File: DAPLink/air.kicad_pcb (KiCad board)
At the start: 2 copper layers, 40.5 x 19.3 mm, 55 parts, among them J1 Conn_01x05, J2 Conn_01x05, J3 Conn_01x04, U1 MT9700, U2 AIR32F103CBT6-LQFP48, U3 RT9013-33GB, U4 USBLC6-2SC6, Y1 8M/20pF

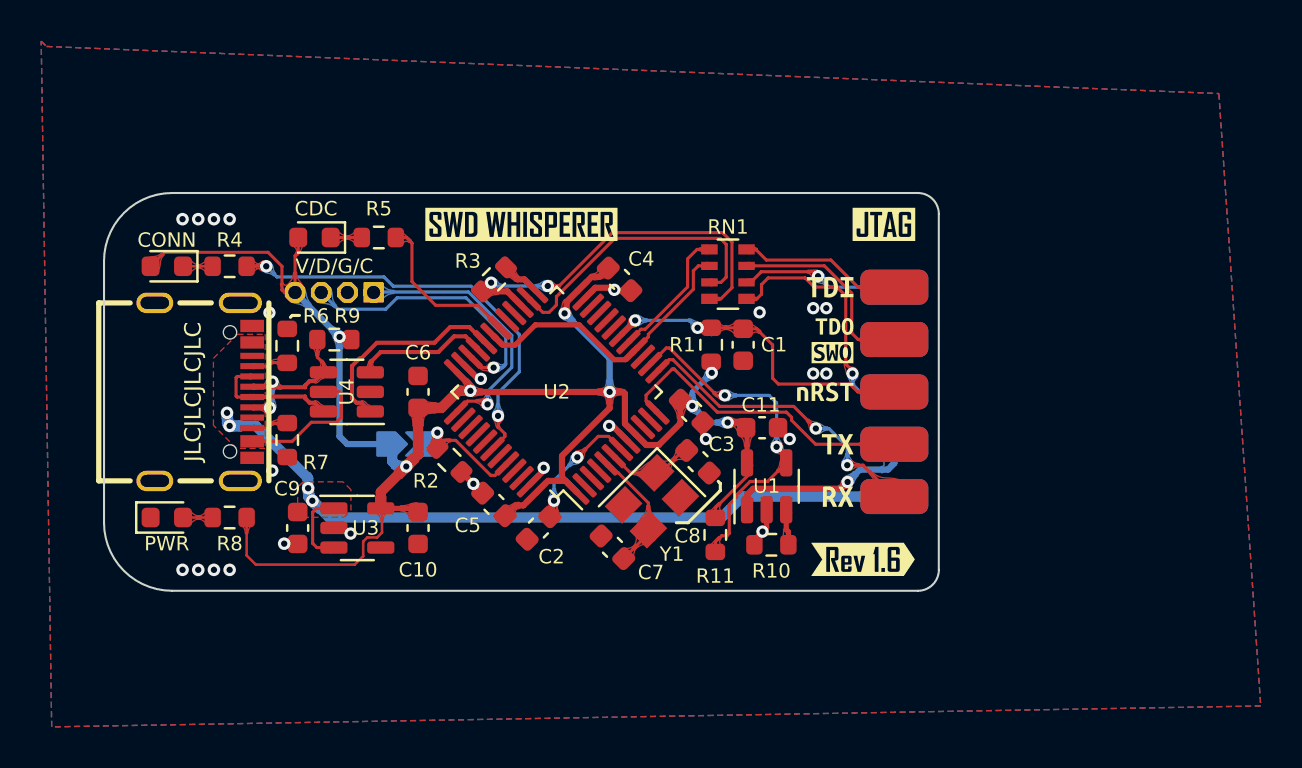
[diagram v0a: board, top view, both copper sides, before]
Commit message: replace Font with specimen/Teko
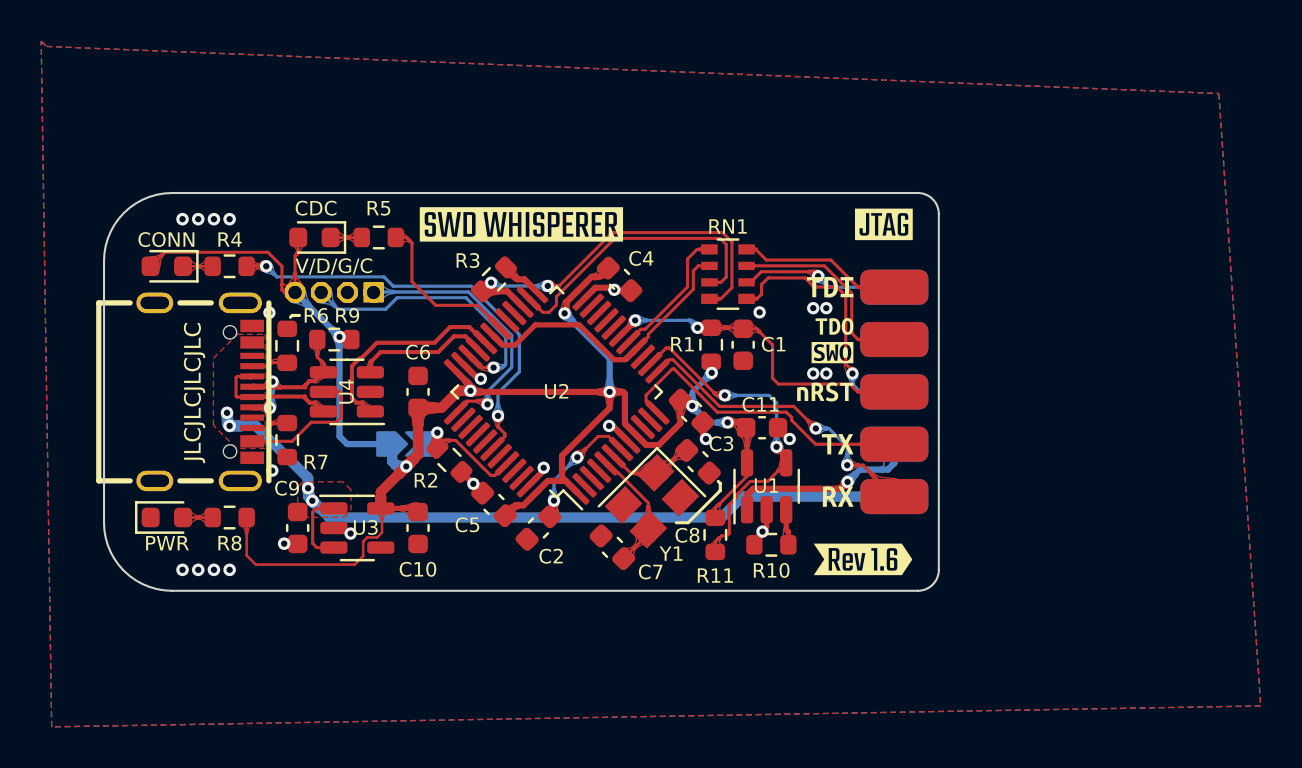
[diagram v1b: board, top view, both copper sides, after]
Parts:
- removed kibuzzard-62F96023: G***, kibuzzard-62F96023
- removed kibuzzard-62F961D8: G***, kibuzzard-62F961D8
- removed kibuzzard-62F9645D: G***, kibuzzard-62F9645D
- removed kibuzzard-6354CD6B: G***, kibuzzard-6354CD6B
- removed kibuzzard-63A8965B: G***, kibuzzard-63A8965B
- added kibuzzard-63E07756: G***, kibuzzard-63E07756, F.Cu at (45.9, 50.3)
- added kibuzzard-63E0775E: G***, kibuzzard-63E0775E, B.Cu at (45.9, 53.1)
- added kibuzzard-63E07768: G***, kibuzzard-63E07768, F.Cu at (63.5, 50.3)
- added kibuzzard-63E07774: G***, kibuzzard-63E07774, B.Cu at (63.5, 50.3)
- added kibuzzard-63E0777D: G***, kibuzzard-63E0777D, F.Cu at (62.5, 66.5)
